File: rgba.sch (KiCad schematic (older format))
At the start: 78 parts, among them J1 USB_C_Receptacle_USB2.0, J10 UART_RTS, J11 Screw 1, J12 Screw 2, J2 BATT CONN, J3 UART_GND, J4 R SPK OUT, J5 L SPK OUT, J6 UART_CTS, J7 UART_VBUS, J8 UART_TX, J9 UART_RX, SW1 POWER/PLAY/PAUSE, SW2 VOL+/NEXT, SW3 VOL-/BACK, U1 FSC-BT806, U2 PCM5242, U3 TPS63001, U4 TPS7A3501, U5 TPS65133DPD, U6 OPA1662

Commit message: new 3.3v voltage regulator and updated a few footprints
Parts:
- removed C30: 0.1uF, Capacitor_SMD:C_0402_1005Metric_Pad0.74x0.62mm_HandSolder, symbol Device:C_Small
- removed R30: 100, Resistor_SMD:R_0402_1005Metric_Pad0.72x0.64mm_HandSolder, symbol Device:R_Small
- removed U3: TPS63001, Package_SON:Texas_DRC0010J_ThermalVias, symbol Regulator_Switching:TPS63001
- added C32: 10uF, Capacitor_SMD:C_0402_1005Metric_Pad0.74x0.62mm_HandSolder, symbol Device:C_Small
- added R31: 453k, Resistor_SMD:R_0402_1005Metric_Pad0.72x0.64mm_HandSolder, symbol Device:R_Small
- added R32: 100k, Resistor_SMD:R_0402_1005Metric_Pad0.72x0.64mm_HandSolder, symbol Device:R_Small
- added U3: TPS62821DLC, Package_DFN_QFN:Texas_VSON-HR-8_1.5x2mm_P0.5mm, symbol Regulator_Switching:TPS62821DLC
- C31: value 0.1uF -> 120pF
- J1: footprint Connector_USB:USB_C_Receptacle_Amphenol_12401610E4-2A -> Connector_USB:USB_C_Receptacle_UJC-HP-3-SMT-TR
- L30: value 2.2uH -> 470nH; footprint Inductor_SMD:L_TDK_VLS3012 -> Inductor_SMD:L_0805_2012Metric_Pad1.05x1.20mm_HandSolder
- renumbered C32 to C30, R31 to R30
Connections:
- wire segments 223 -> 213
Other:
- moved on the sheet: C30, D30, R30

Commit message: start working on new regulator
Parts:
- removed C32: 10uF, Capacitor_SMD:C_0402_1005Metric_Pad0.74x0.62mm_HandSolder, symbol Device:C_Small
- removed R31: 453k, Resistor_SMD:R_0402_1005Metric_Pad0.72x0.64mm_HandSolder, symbol Device:R_Small
- removed R32: 100k, Resistor_SMD:R_0402_1005Metric_Pad0.72x0.64mm_HandSolder, symbol Device:R_Small
- removed U3: TPS62821DLC, Package_DFN_QFN:Texas_VSON-HR-8_1.5x2mm_P0.5mm, symbol Regulator_Switching:TPS62821DLC
- added U3: TPS62849DLCR, SON50P200X150X100-8N, symbol TPS62849DLCR:TPS62849DLCR
- C31: value 120pF -> 10uF
- J2: symbol Connector:Conn_01x02_Male -> Connector:JST_2Pin
- L30: value 470nH -> 2.2uH
- U2: symbol Audio:PCM5242 -> Audio:PCM5242_HW_CTRL
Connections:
- net +1V8: now also U3.4 (EN)
- net +3V3: now also U3.8 (VOS)
- net GND: now also C31.2, U3.1 (GND), U3.3 (MODE), U3.5 (VSET), U3.6 (STOP); no longer J1.S1 (SHIELD), J4.3 (Pin_3), J5.3 (Pin_3)
- net at C30.1, D30.1 (K): now also U3.2 (VIN)
- net at L30.1: now also U3.7 (SW)
- no-connect marks 39 -> 42
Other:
- moved on the sheet: D30, R30

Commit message: rev 1.1
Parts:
- C10, C20, C21, C22, C23, C24, C25, C26, C27, C30, C31, C40, C41, C42, C50, C51, C52, C53, C600, C601, C602, C603, C610, C611, C612, C620, C621, C625, D1, D2, D30, L50, L51: Source (none) -> https://www.mouser.com/ProjectManager/ProjectDetail.aspx?Ac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
- J1: value USB_C_Receptacle_USB2.0 -> CHARGE CONN; footprint Connector_USB:USB_C_Receptacle_UJC-HP-3-SMT-TR -> rgba:USB_C_Receptacle_UJC-HP-3-SMT-TR; symbol Connector:USB_C_Receptacle_USB2.0 -> rgba:USB_C_Receptacle_PowerOnly; Source (none) -> https://www.mouser.com/ProjectManager/ProjectDetail.aspx?Ac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
- J11: footprint MountingHole:MountingHole_2.2mm_M2_Pad_Via -> rgba:MountingHole_1.2mm_M1_Pad; Source (none) -> https://www.mouser.com/ProjectManager/ProjectDetail.aspx?Ac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
- J12: value Screw 2 -> Screw 1; footprint MountingHole:MountingHole_2.2mm_M2_Pad_Via -> rgba:MountingHole_1.2mm_M1_Pad; Source (none) -> https://www.mouser.com/ProjectManager/ProjectDetail.aspx?Ac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
- J2: footprint Connector_JST:JST_PH_S2B-PH-SM4-TB_1x02-1MP_P2.00mm_Horizontal -> Connector_JST:JST_ACH_BM02B-ACHSS-GAN-ETF_1x02-1MP_P1.20mm_Vertical; Source (none) -> https://www.digikey.com/en/products/detail/jst-sales-americ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
- L30: value 2.2uH -> 4.7uH; footprint Inductor_SMD:L_0805_2012Metric_Pad1.05x1.20mm_HandSolder -> Inductor_SMD:L_1008_2520Metric_Pad1.43x2.20mm_HandSolder; Source (none) -> https://www.mouser.com/ProjectManager/ProjectDetail.aspx?Ac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
- LED1: renamed from D3; value RED -> ORNG; footprint LED_SMD:LED_0402_1005Metric_Pad0.77x0.64mm_HandSolder -> LED_SMD:LED_0603_1608Metric_Castellated; Source (none) -> https://www.mouser.com/ProjectManager/ProjectDetail.aspx?Ac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
- LED2: renamed from D4; footprint LED_SMD:LED_0402_1005Metric_Pad0.77x0.64mm_HandSolder -> LED_SMD:LED_0603_1608Metric_Castellated; Source (none) -> https://www.mouser.com/ProjectManager/ProjectDetail.aspx?Ac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
- LED3: renamed from D5; value GREEN -> WHITE; footprint LED_SMD:LED_0402_1005Metric_Pad0.77x0.64mm_HandSolder -> LED_SMD:LED_0603_1608Metric_Castellated; Source (none) -> https://www.mouser.com/ProjectManager/ProjectDetail.aspx?Ac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
- R1, R2, R3, R610, R611, R620, R621: value 1k -> 1K; Source (none) -> https://www.mouser.com/ProjectManager/ProjectDetail.aspx?Ac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
- R10, R11, R30: value 100k -> 100K; Source (none) -> https://www.mouser.com/ProjectManager/ProjectDetail.aspx?Ac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
- R22, R614, R615, R624: value 68 -> 68R; Source (none) -> https://www.mouser.com/ProjectManager/ProjectDetail.aspx?Ac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
- R612, R613, R622, R623: value 4.7k -> 4.7K; Source (none) -> https://www.mouser.com/ProjectManager/ProjectDetail.aspx?Ac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
- SW1: value POWER/PLAY/PAUSE -> Switch_RA; footprint SamacSys_Parts:TL4110AF160Q -> rgba:TL4110AF160Q; Source (none) -> https://www.mouser.com/ProjectManager/ProjectDetail.aspx?Ac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
- SW2: value VOL+/NEXT -> Switch_RA; footprint SamacSys_Parts:TL4110AF160Q -> rgba:TL4110AF160Q; Source (none) -> https://www.mouser.com/ProjectManager/ProjectDetail.aspx?Ac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
- SW3: value VOL-/BACK -> Switch_RA; footprint SamacSys_Parts:TL4110AF160Q -> rgba:TL4110AF160Q; Source (none) -> https://www.mouser.com/ProjectManager/ProjectDetail.aspx?Ac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
- U1: footprint Feasycom:FSC-BT806 -> rgba:FSC-BT806; symbol feasycom:FSC-BT806 -> rgba:FSC-BT806; Source (none) -> https://www.aliexpress.com/i/4000096888920.html
- U2: footprint Package_DFN_QFN:QFN-32-1EP_5x5mm_P0.5mm_EP3.45x3.45mm -> rgba:QFN-32-1EP_5x5mm_P0.5mm_EP3.45x3.45mm; symbol Audio:PCM5242_HW_CTRL -> rgba:PCM5242_HW_CTRL; Source (none) -> https://www.mouser.com/ProjectManager/ProjectDetail.aspx?Ac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
- U3: footprint SON50P200X150X100-8N -> rgba:VSON-8_1.5x2mm_P0.5mm; symbol TPS62849DLCR:TPS62849DLCR -> rgba:TPS62849DLCR; Package SON50P200X150X100-8N -> DLC0008B; Source (none) -> https://www.mouser.com/ProjectManager/ProjectDetail.aspx?Ac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
- U4: footprint Package_SON:WSON-6-1EP_2x2mm_P0.65mm_EP1x1.6mm_ThermalVias -> rgba:WSON-6-1EP_2x2mm_P0.65mm_EP1x1.6mm_ThermalVias; symbol Regulator_Linear:TPS7A3501 -> rgba:TPS7A3501; Source (none) -> https://www.mouser.com/ProjectManager/ProjectDetail.aspx?Ac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
- U5: footprint Package_SON:WSON-12-1EP_3x3mm_P0.45mm_EP1.2x2mm -> rgba:WSON-12-1EP_3x3mm_P0.45mm_EP1.2x2mm; symbol Regulator_Switching:TPS65133DPD -> rgba:TPS65133DPD; Source (none) -> https://www.mouser.com/ProjectManager/ProjectDetail.aspx?Ac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
- U6: footprint Package_SO:VSSOP-8_3.0x3.0mm_P0.65mm -> rgba:VSSOP-8_3.0x3.0mm_P0.65mm; Source (none) -> https://www.mouser.com/ProjectManager/ProjectDetail.aspx?Ac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
- U6: footprint Package_SO:VSSOP-8_3.0x3.0mm_P0.65mm -> rgba:VSSOP-8_3.0x3.0mm_P0.65mm; symbol Amplifier_Audio:OPA1662 -> rgba:OPA1662; Source (none) -> https://www.mouser.com/ProjectManager/ProjectDetail.aspx?Ac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
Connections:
- net GND: now also J1.S1 (SHIELD); no longer J1.A12 (GND), J1.B12 (GND)
- net VBUS: no longer J1.A4 (VBUS), J1.B4 (VBUS)
- net PIO6 renamed VOL+_NEXT
- net PIO7 renamed VOL-_PREV
- no-connect marks 42 -> 35
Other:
- note added: "Power/Play/Pause"
- moved on the sheet: D1, D2, J11, J2, LED1, LED2, LED3, R1, R2, R3, SW1, SW2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

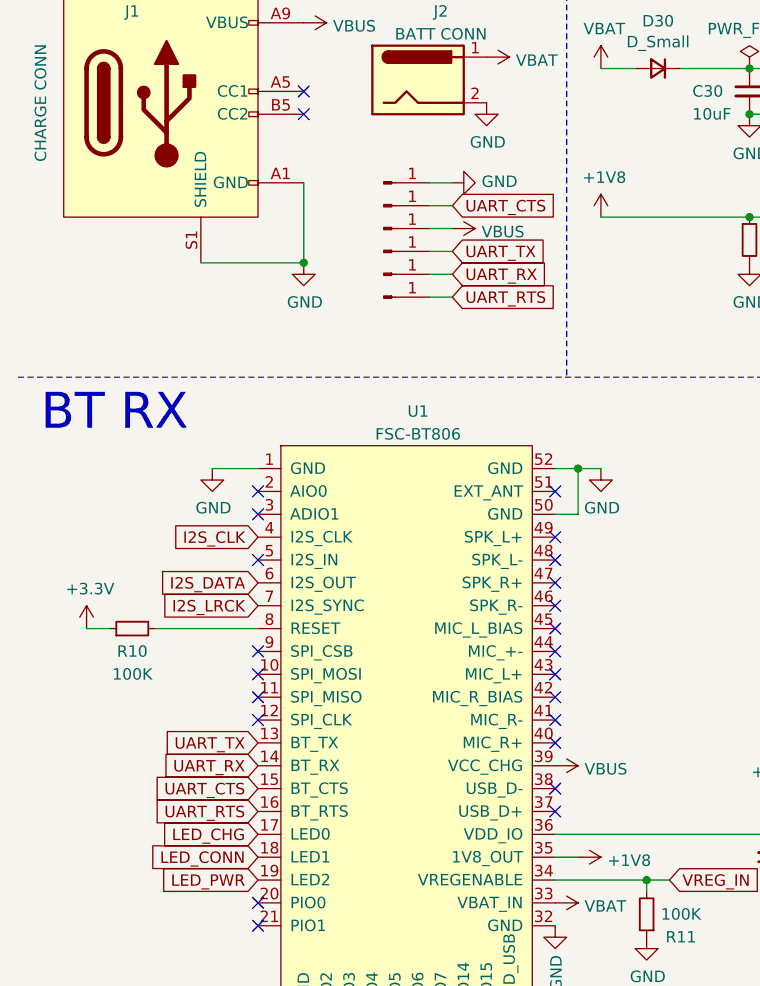
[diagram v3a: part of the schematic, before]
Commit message: modify uart header and led position
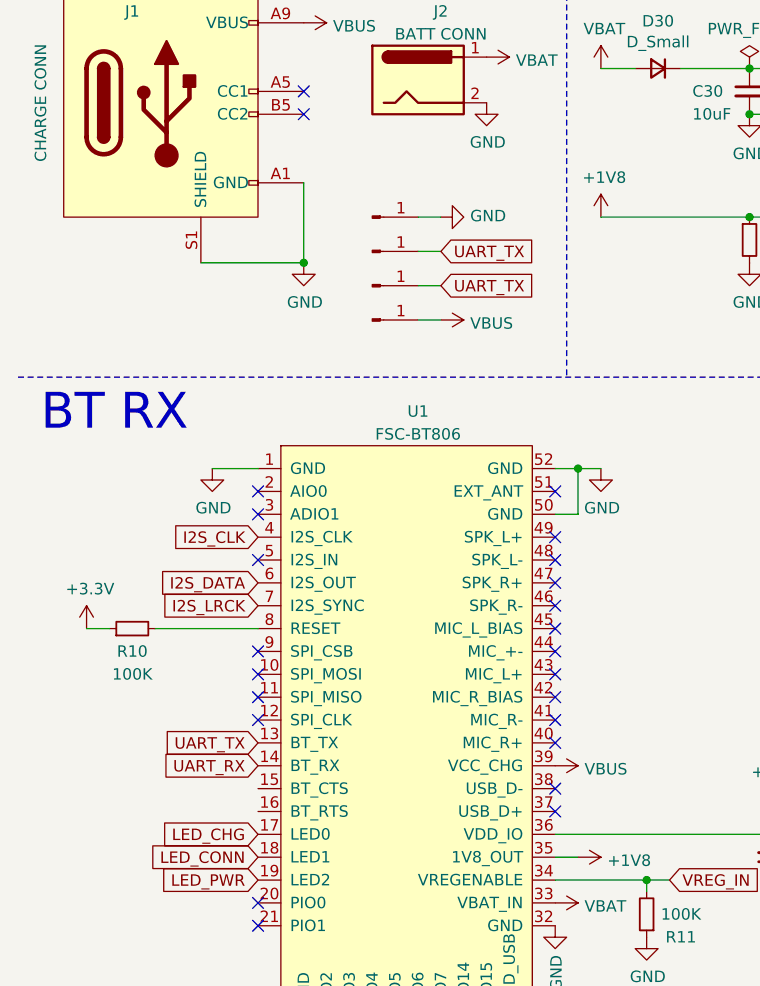
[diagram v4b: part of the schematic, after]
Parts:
- removed J10: UART_RTS, TestPoint:TestPoint_THTPad_D1.0mm_Drill0.5mm, symbol Connector:Conn_01x01_Male
- removed J6: UART_CTS, TestPoint:TestPoint_THTPad_D1.0mm_Drill0.5mm, symbol Connector:Conn_01x01_Male
- removed J9: UART_RX, TestPoint:TestPoint_THTPad_D1.0mm_Drill0.5mm, symbol Connector:Conn_01x01_Male
- added J?: UART_TX, TestPoint:TestPoint_THTPad_D1.0mm_Drill0.5mm, symbol Connector:Conn_01x01_Male
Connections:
- net UART_TX: now also J?.1 (Pin_1)
- net UART_CTS: no longer names the net of U1.15 (BT_CTS)
- net UART_RTS: no longer names the net of U1.16 (BT_RTS)
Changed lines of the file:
@@
 Text GLabel 1500 4200 0    50   Input ~ 0
 UART_RX
-Text GLabel 1500 4300 0    50   Input ~ 0
-UART_CTS
-Text GLabel 1500 4400 0    50   Input ~ 0
-UART_RTS
 Text GLabel 1500 4500 0    50   Input ~ 0
 LED_CHG
@@
 L power:VBUS #PWR0158
 U 1 1 60DC8673
-P 2350 1850
-F 0 "#PWR0158" H 2350 1700 50  0001 C CNN
-F 1 "VBUS" V 2365 1978 50  0000 L CNN
-F 2 "" H 2350 1850 50  0001 C CNN
-F 3 "" H 2350 1850 50  0001 C CNN
-	1    2350 1850
+P 2300 2250
+F 0 "#PWR0158" H 2300 2100 50  0001 C CNN
+F 1 "VBUS" V 2315 2378 50  0000 L CNN
+F 2 "" H 2300 2250 50  0001 C CNN
+F 3 "" H 2300 2250 50  0001 C CNN
+	1    2300 2250
 	0    1    1    0
 $EndComp
-Text GLabel 2350 1750 2    50   Input ~ 0
-UART_CTS
-Text GLabel 2350 1950 2    50   Input ~ 0
+Text GLabel 2300 2100 2    50   Input ~ 0
 UART_TX
-Text GLabel 2350 2050 2    50   Input ~ 0
-UART_RX
-Text GLabel 2350 2150 2    50   Input ~ 0
-UART_RTS
-Wire Wire Line
-	2250 1750 2350 1750
-Wire Wire Line
-	2250 1850 2350 1850
-Wire Wire Line
-	2250 1950 2350 1950
-Wire Wire Line
-	2250 2050 2350 2050
-Wire Wire Line
-	2250 2150 2350 2150
+Wire Wire Line
+	2200 2250 2300 2250
+Wire Wire Line
+	2200 2100 2300 2100
 Text Notes 4850 6250 0    157  ~ 0
 OUT CONN
@@
 $EndComp
 Wire Wire Line
-	2250 1650 2350 1650
+	2200 1800 2300 1800
 $Comp
 L power:GND #PWR0157
 U 1 1 60DC8022
-P 2350 1650
-F 0 "#PWR0157" H 2350 1400 50  0001 C CNN
-F 1 "GND" V 2355 1522 50  0000 R CNN
-F 2 "" H 2350 1650 50  0001 C CNN
-F 3 "" H 2350 1650 50  0001 C CNN
-	1    2350 1650
+P 2300 1800
+F 0 "#PWR0157" H 2300 1550 50  0001 C CNN
+F 1 "GND" V 2305 1672 50  0000 R CNN
+F 2 "" H 2300 1800 50  0001 C CNN
+F 3 "" H 2300 1800 50  0001 C CNN
+	1    2300 1800
 	0    -1   -1   0
 $EndComp
@@
 L Connector:Conn_01x01_Male J3
 U 1 1 6087C91C
-P 2050 1650
-F 0 "J3" H 2158 1739 50  0001 C CNN
-F 1 "UART_GND" H 2158 1740 50  0001 C CNN
-F 2 "TestPoint:TestPoint_THTPad_D1.0mm_Drill0.5mm" H 2050 1650 50  0001 C CNN
-F 3 "~" H 2050 1650 50  0001 C CNN
-	1    2050 1650
-	1    0    0    -1
-$EndComp
-$Comp
-L Connector:Conn_01x01_Male J6
-U 1 1 6087D420
-P 2050 1750
-F 0 "J6" H 2158 1839 50  0001 C CNN
-F 1 "UART_CTS" H 2158 1840 50  0001 C CNN
-F 2 "TestPoint:TestPoint_THTPad_D1.0mm_Drill0.5mm" H 2050 1750 50  0001 C CNN
-F 3 "~" H 2050 1750 50  0001 C CNN
-	1    2050 1750
+P 2000 1800
+F 0 "J3" H 2108 1889 50  0001 C CNN
+F 1 "UART_GND" H 2108 1890 50  0001 C CNN
+F 2 "TestPoint:TestPoint_THTPad_D1.0mm_Drill0.5mm" H 2000 1800 50  0001 C CNN
+F 3 "~" H 2000 1800 50  0001 C CNN
+	1    2000 1800
 	1    0    0    -1
 $EndComp
@@
 L Connector:Conn_01x01_Male J7
 U 1 1 6087D606
-P 2050 1850
-F 0 "J7" H 2158 1939 50  0001 C CNN
-F 1 "UART_VBUS" H 2158 1940 50  0001 C CNN
-F 2 "TestPoint:TestPoint_THTPad_D1.0mm_Drill0.5mm" H 2050 1850 50  0001 C CNN
-F 3 "~" H 2050 1850 50  0001 C CNN
-	1    2050 1850
+P 2000 2250
+F 0 "J7" H 2108 2339 50  0001 C CNN
+F 1 "UART_VBUS" H 2108 2340 50  0001 C CNN
+F 2 "TestPoint:TestPoint_THTPad_D1.0mm_Drill0.5mm" H 2000 2250 50  0001 C CNN
+F 3 "~" H 2000 2250 50  0001 C CNN
+	1    2000 2250
 	1    0    0    -1
 $EndComp
@@
 L Connector:Conn_01x01_Male J8
 U 1 1 6087D7EB
-P 2050 1950
-F 0 "J8" H 2158 2039 50  0001 C CNN
-F 1 "UART_TX" H 2158 2040 50  0001 C CNN
-F 2 "TestPoint:TestPoint_THTPad_D1.0mm_Drill0.5mm" H 2050 1950 50  0001 C CNN
-F 3 "~" H 2050 1950 50  0001 C CNN
-	1    2050 1950
-	1    0    0    -1
-$EndComp
-$Comp
-L Connector:Conn_01x01_Male J9
-U 1 1 6087D92E
-P 2050 2050
-F 0 "J9" H 2158 2139 50  0001 C CNN
-F 1 "UART_RX" H 2158 2140 50  0001 C CNN
-F 2 "TestPoint:TestPoint_THTPad_D1.0mm_Drill0.5mm" H 2050 2050 50  0001 C CNN
-F 3 "~" H 2050 2050 50  0001 C CNN
-	1    2050 2050
-	1    0    0    -1
-$EndComp
-$Comp
-L Connector:Conn_01x01_Male J10
-U 1 1 6087DAE4
-P 2050 2150
-F 0 "J10" H 2158 2239 50  0001 C CNN
-F 1 "UART_RTS" H 2158 2240 50  0001 C CNN
-F 2 "TestPoint:TestPoint_THTPad_D1.0mm_Drill0.5mm" H 2050 2150 50  0001 C CNN
-F 3 "~" H 2050 2150 50  0001 C CNN
-	1    2050 2150
+P 2000 2100
+F 0 "J8" H 2108 2189 50  0001 C CNN
+F 1 "UART_TX" H 2108 2190 50  0001 C CNN
+F 2 "TestPoint:TestPoint_THTPad_D1.0mm_Drill0.5mm" H 2000 2100 50  0001 C CNN
+F 3 "~" H 2000 2100 50  0001 C CNN
+	1    2000 2100
 	1    0    0    -1
 $EndComp
@@
 	1    0    0    -1
 $EndComp
+Text GLabel 2300 1950 2    50   Input ~ 0
+UART_TX
+Wire Wire Line
+	2200 1950 2300 1950
+$Comp
+L Connector:Conn_01x01_Male J?
+U 1 1 606EF0A8
+P 2000 1950
+F 0 "J?" H 2108 2039 50  0001 C CNN
+F 1 "UART_TX" H 2108 2040 50  0001 C CNN
+F 2 "TestPoint:TestPoint_THTPad_D1.0mm_Drill0.5mm" H 2000 1950 50  0001 C CNN
+F 3 "~" H 2000 1950 50  0001 C CNN
+	1    2000 1950
+	1    0    0    -1
+$EndComp

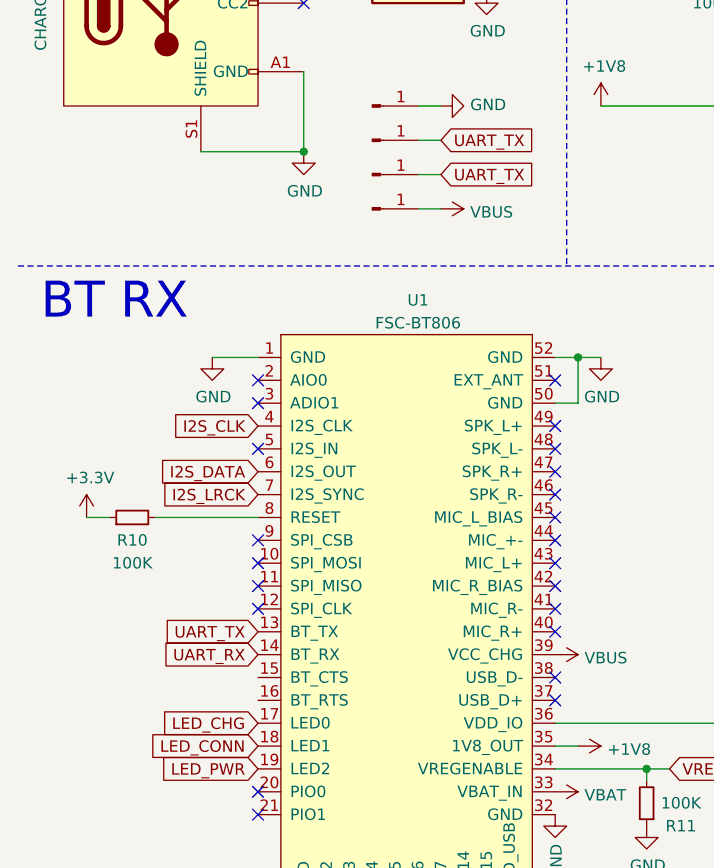
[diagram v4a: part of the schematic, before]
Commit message: more size optimization
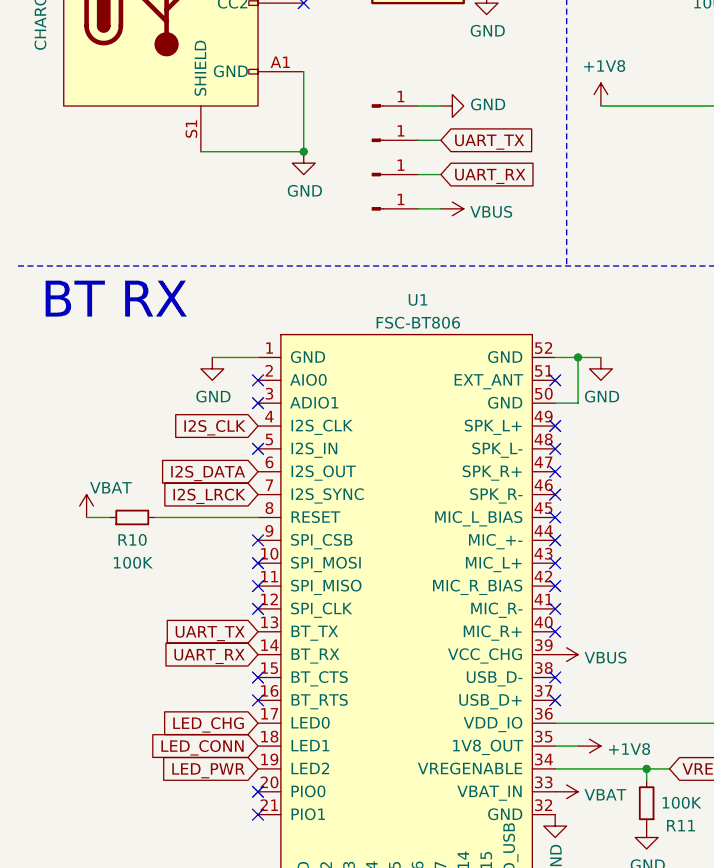
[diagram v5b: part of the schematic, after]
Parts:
- J8: value UART_TX -> UART_RX
- gave numbers to parts that had none: 1
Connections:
- net +3V3: no longer R10.1
- net UART_RX: now also J8.1 (Pin_1)
- net UART_TX: no longer J8.1 (Pin_1)
- net VBAT: now also R10.1
- no-connect marks 35 -> 37
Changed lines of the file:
@@
 Connection ~ 3750 4500
-$Comp
-L power:+3.3V #PWR0151
-U 1 1 609230D8
-P 750 3600
-F 0 "#PWR0151" H 750 3450 50  0001 C CNN
-F 1 "+3.3V" H 765 3773 50  0000 C CNN
-F 2 "" H 750 3600 50  0001 C CNN
-F 3 "" H 750 3600 50  0001 C CNN
-	1    750  3600
-	1    0    0    -1
-$EndComp
 $Comp
 L Device:R_Small R10
@@
 $EndComp
 Text GLabel 2300 2100 2    50   Input ~ 0
-UART_TX
+UART_RX
 Wire Wire Line
 	2200 2250 2300 2250
@@
 P 2000 2100
 F 0 "J8" H 2108 2189 50  0001 C CNN
-F 1 "UART_TX" H 2108 2190 50  0001 C CNN
+F 1 "UART_RX" H 2108 2190 50  0001 C CNN
 F 2 "TestPoint:TestPoint_THTPad_D1.0mm_Drill0.5mm" H 2000 2100 50  0001 C CNN
 F 3 "~" H 2000 2100 50  0001 C CNN
@@
 	2200 1950 2300 1950
 $Comp
-L Connector:Conn_01x01_Male J?
+L Connector:Conn_01x01_Male J6
 U 1 1 606EF0A8
 P 2000 1950
-F 0 "J?" H 2108 2039 50  0001 C CNN
+F 0 "J6" H 2108 2039 50  0001 C CNN
 F 1 "UART_TX" H 2108 2040 50  0001 C CNN
 F 2 "TestPoint:TestPoint_THTPad_D1.0mm_Drill0.5mm" H 2000 1950 50  0001 C CNN
@@
 	1    0    0    -1
 $EndComp
+$Comp
+L power:VBAT #PWR0131
+U 1 1 607CBF3B
+P 750 3600
+F 0 "#PWR0131" H 400 3500 50  0001 C CNN
+F 1 "VBAT" H 765 3728 50  0000 L CNN
+F 2 "" H 750 3600 50  0001 C CNN
+F 3 "" H 750 3600 50  0001 C CNN
+	1    750  3600
+	1    0    0    -1
+$EndComp
+NoConn ~ 1500 4400
+NoConn ~ 1500 4300
 $EndSCHEMATC

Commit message: make UART terminals larger
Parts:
- J3, J6, J7, J8: footprint TestPoint:TestPoint_THTPad_D1.0mm_Drill0.5mm -> TestPoint:TestPoint_THTPad_D1.5mm_Drill0.7mm
- J4, J5: footprint Connector_Wire:SolderWire-0.1sqmm_1x03_P3.6mm_D0.4mm_OD1mm -> rgba:SolderWire_AudioOut_1x03_P2.0mm
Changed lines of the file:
@@
 F 0 "J4" H 5150 7100 50  0000 C CNN
 F 1 "R SPK OUT" H 5150 7000 50  0000 C CNN
-F 2 "Connector_Wire:SolderWire-0.1sqmm_1x03_P3.6mm_D0.4mm_OD1mm" H 5200 6800 50  0001 C CNN
+F 2 "rgba:SolderWire_AudioOut_1x03_P2.0mm" H 5200 6800 50  0001 C CNN
 F 3 "~" H 5200 6800 50  0001 C CNN
 	1    5200 6800
@@
 F 0 "J5" H 5150 7700 50  0000 C CNN
 F 1 "L SPK OUT" H 5150 7600 50  0000 C CNN
-F 2 "Connector_Wire:SolderWire-0.1sqmm_1x03_P3.6mm_D0.4mm_OD1mm" H 5200 7400 50  0001 C CNN
+F 2 "rgba:SolderWire_AudioOut_1x03_P2.0mm" H 5200 7400 50  0001 C CNN
 F 3 "~" H 5200 7400 50  0001 C CNN
 	1    5200 7400
@@
 F 0 "J3" H 2108 1889 50  0001 C CNN
 F 1 "UART_GND" H 2108 1890 50  0001 C CNN
-F 2 "TestPoint:TestPoint_THTPad_D1.0mm_Drill0.5mm" H 2000 1800 50  0001 C CNN
+F 2 "TestPoint:TestPoint_THTPad_D1.5mm_Drill0.7mm" H 2000 1800 50  0001 C CNN
 F 3 "~" H 2000 1800 50  0001 C CNN
 	1    2000 1800
@@
 F 0 "J7" H 2108 2339 50  0001 C CNN
 F 1 "UART_VBUS" H 2108 2340 50  0001 C CNN
-F 2 "TestPoint:TestPoint_THTPad_D1.0mm_Drill0.5mm" H 2000 2250 50  0001 C CNN
+F 2 "TestPoint:TestPoint_THTPad_D1.5mm_Drill0.7mm" H 2000 2250 50  0001 C CNN
 F 3 "~" H 2000 2250 50  0001 C CNN
 	1    2000 2250
@@
 F 0 "J8" H 2108 2189 50  0001 C CNN
 F 1 "UART_RX" H 2108 2190 50  0001 C CNN
-F 2 "TestPoint:TestPoint_THTPad_D1.0mm_Drill0.5mm" H 2000 2100 50  0001 C CNN
+F 2 "TestPoint:TestPoint_THTPad_D1.5mm_Drill0.7mm" H 2000 2100 50  0001 C CNN
 F 3 "~" H 2000 2100 50  0001 C CNN
 	1    2000 2100
@@
 F 0 "J6" H 2108 2039 50  0001 C CNN
 F 1 "UART_TX" H 2108 2040 50  0001 C CNN
-F 2 "TestPoint:TestPoint_THTPad_D1.0mm_Drill0.5mm" H 2000 1950 50  0001 C CNN
+F 2 "TestPoint:TestPoint_THTPad_D1.5mm_Drill0.7mm" H 2000 1950 50  0001 C CNN
 F 3 "~" H 2000 1950 50  0001 C CNN
 	1    2000 1950
